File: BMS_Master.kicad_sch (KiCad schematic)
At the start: 24 parts, among them U1 STM32F103C8Tx, U2 AP2204K-ADJ, U3 AP2204K-ADJ, Y1 32.768k, Y2 8M

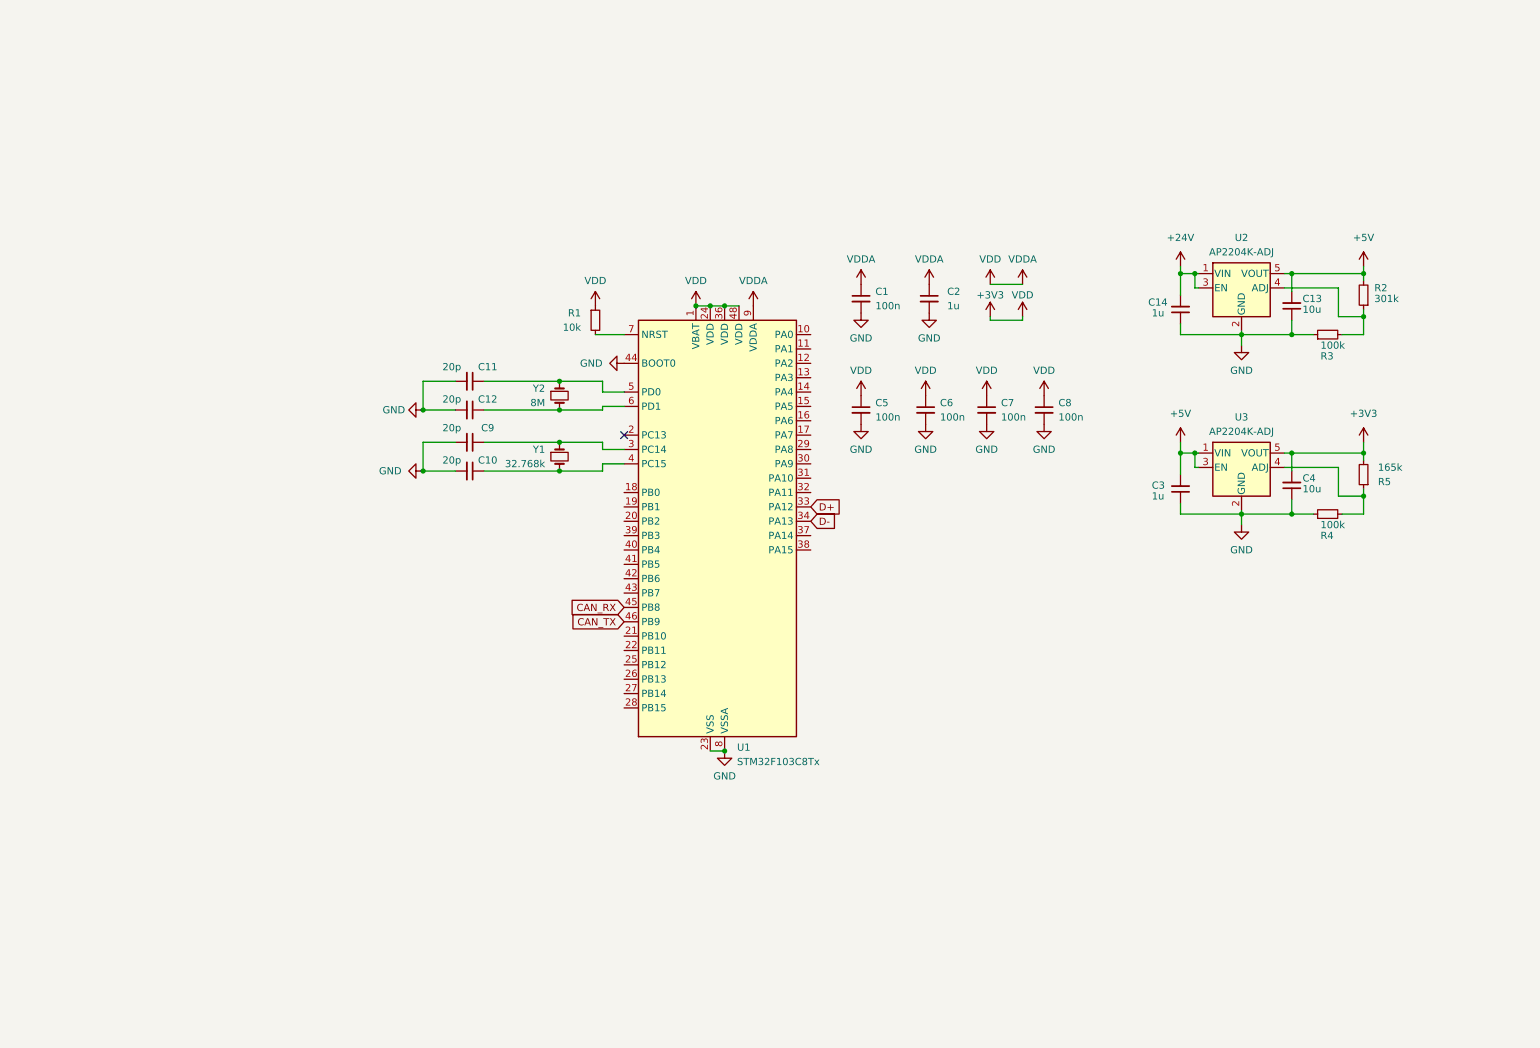
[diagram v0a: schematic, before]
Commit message: Add can bus transeiver and Readme.md
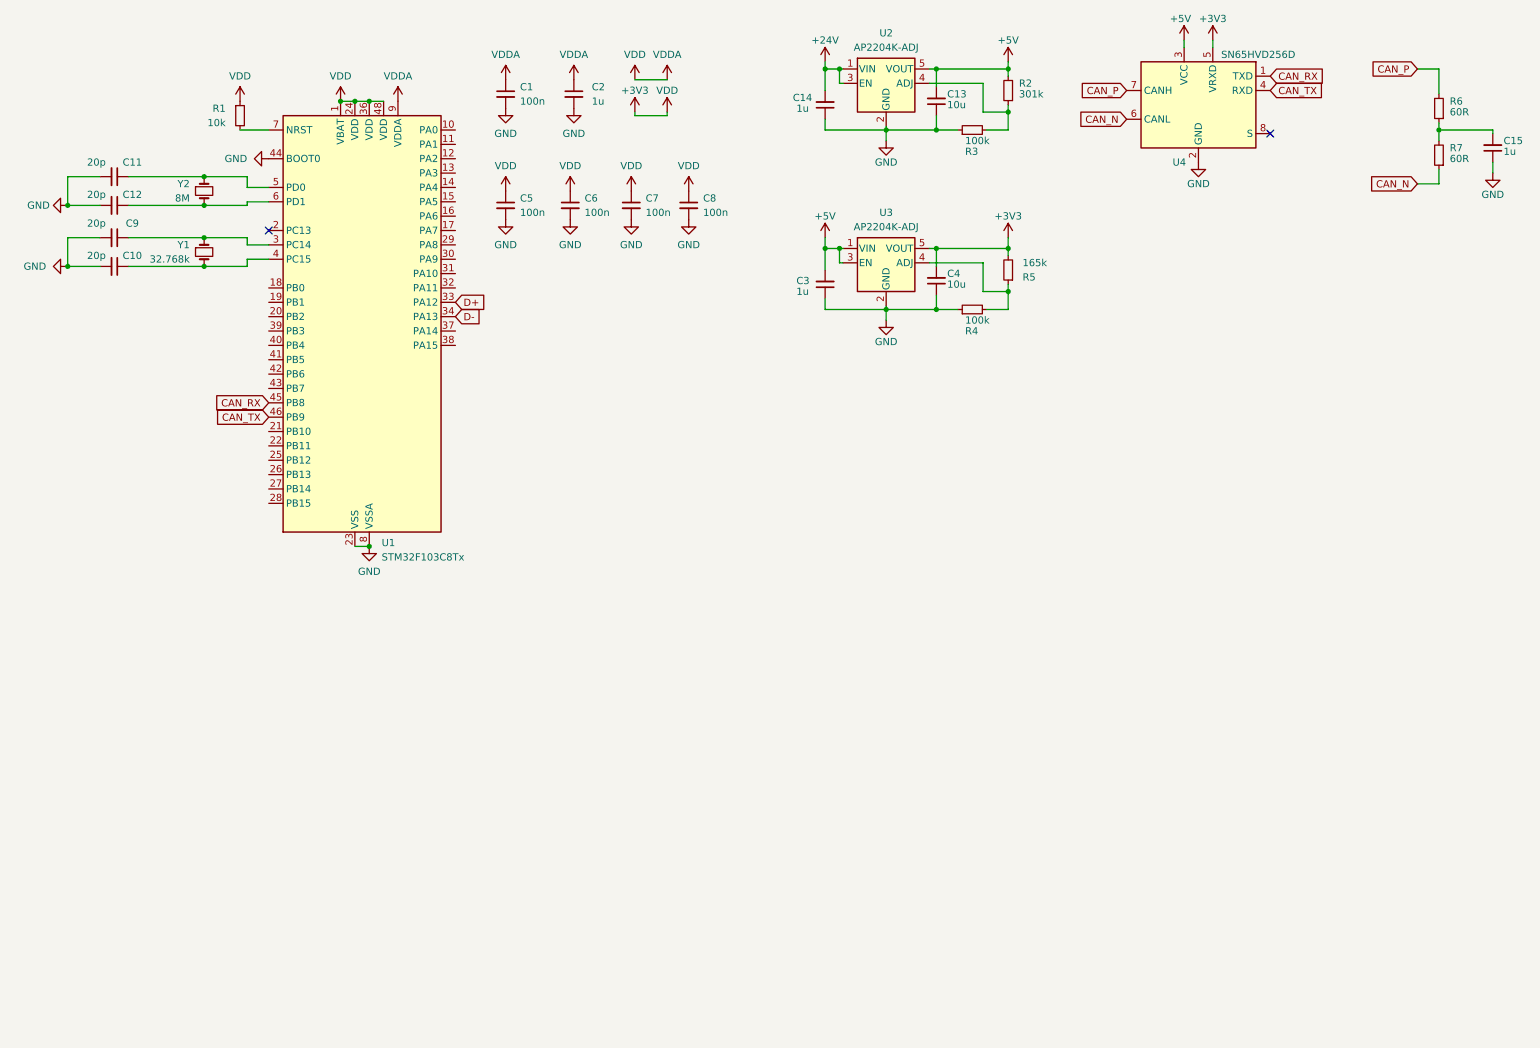
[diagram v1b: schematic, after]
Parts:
- added C15: 1u, Capacitor_SMD:C_0805_2012Metric, symbol Device:C_Small
- added R6, R7: 60R, Resistor_SMD:R_0603_1608Metric, symbol Device:R_Small
- added U4: SN65HVD256D, Package_SO:SOIC-8_3.9x4.9mm_P1.27mm, symbol Interface_CAN_LIN:SN65HVD256D
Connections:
- net +3V3: now also U4.5 (VRXD)
- net +5V: now also U4.3 (VCC)
- net CAN_RX: now also U4.1 (TXD)
- net CAN_TX: now also U4.4 (RXD)
- net GND: now also C15.1, U4.2 (GND)
- new net: C15.2, R6.1, R7.2
- new net CAN_N: R7.1, U4.6 (CANL)
- new net CAN_P: R6.2, U4.7 (CANH)
- no-connect marks 1 -> 2
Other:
- moved on the sheet: C1, C10, C11, C12, C13, C14, C2, C3, C4, C5, C6, C7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

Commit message: Finish schematic (probably)
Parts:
- added C16, C17: 220n, Capacitor_SMD:C_0805_2012Metric, symbol Device:C_Small
- added C18, C19, C22, C23: 220p, Capacitor_SMD:C_0603_1608Metric, symbol Device:C_Small
- added C20, C21: 100p, Capacitor_SMD:C_0603_1608Metric, symbol Device:C_Small
- added J1: BMS_M_OUT, Connector_Molex:Molex_Micro-Fit_3.0_43650-0200_1x02_P3.00mm_Horizontal, symbol Connector_Generic:Conn_01x02
- added J2: BMS_M_IN, Connector_Molex:Molex_Micro-Fit_3.0_43650-0200_1x02_P3.00mm_Horizontal, symbol Connector_Generic:Conn_01x02
- added J3: PWR, Connector_JST:JST_XH_S2B-XH-A_1x02_P2.50mm_Horizontal, symbol Connector_Generic:Conn_01x02
- added J4: CAN, Connector_JST:JST_XH_S3B-XH-A_1x03_P2.50mm_Horizontal, symbol Connector_Generic:Conn_01x03
- added J5: PROG, Connector_JST:JST_XH_S3B-XH-A_1x03_P2.50mm_Horizontal, symbol Connector_Generic:Conn_01x03
- added R10, R8, R9: 60R, Resistor_SMD:R_0603_1608Metric, symbol Device:R_Small
- added R11, R16: 1k, Resistor_SMD:R_0603_1608Metric, symbol Device:R_Small
- added R12, R13, R14, R15: 49R, Resistor_SMD:R_0603_1608Metric, symbol Device:R_Small
- added SW1: SW_SPST, symbol Switch:SW_SPST
- added TR1, TR2: Wuerth_750319696, Transformer_SMD:Transformer_Wuerth_750315371, symbol Transformer:Wuerth_750315371
- added U5: BQ79600-Q1, Package_SO:TSSOP-16_4.4x5mm_P0.65mm, symbol Local_Lib:BQ79600-Q1
- C1: footprint Capacitor_SMD:C_0805_2012Metric -> Package_SO:TSSOP-16-1EP_4.4x5mm_P0.65mm
- Y1, Y2: footprint (none) -> Crystal:Crystal_SMD_SeikoEpson_FA238-4Pin_3.2x2.5mm
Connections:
- net +24V: now also J3.1 (Pin_1), U5. (nUART/SPI(SPI_RDY))
- net CAN_N: now also J4.1 (Pin_1)
- net CAN_P: now also J4.3 (Pin_3)
- net D+: now also U1.32 (PA11); no longer U1.33 (PA12)
- net D-: now also U1.33 (PA12); no longer U1.34 (PA13)
- net GND: now also C16.2, C17.1, J3.2 (Pin_2), J5.3 (Pin_3), SW1.1 (A), U5. (nUART/SPI(SPI_RDY))
- net at R1.2, U1.7 (NRST): now also SW1.2 (B)
- net SWCLK: now reaches U1.37 (PA14)
- net SWCLK: now also J5.2 (Pin_2)
- new net: R13.2, TR2.3
- new net: R14.2, TR1.1
- new net: C20.1, TR1.2
- new net: R15.2, TR1.3
- new net: J1.2 (Pin_2), TR1.4
- new net: J1.1 (Pin_1), TR1.6
- new net: C16.1, U5. (nUART/SPI(SPI_RDY))
- new net: C17.2, U5. (nUART/SPI(SPI_RDY))
- new net: C21.1, TR2.2
- new net: J2.1 (Pin_1), TR2.6
- new net: J2.2 (Pin_2), TR2.4
- new net: R12.2, TR2.1
- new net COMHN: C23.1, R15.1, R16.2, U5. (nUART/SPI(SPI_RDY))
- new net COMHP: C22.1, R14.1, R16.1, U5. (nUART/SPI(SPI_RDY))
- new net COMLN: C19.1, R11.2, R13.1, U5. (nUART/SPI(SPI_RDY))
- new net COMLP: C18.1, R11.1, R12.1, U5. (nUART/SPI(SPI_RDY))
- new net GND1: C18.2, C19.2, C20.2, C21.2, C22.2, C23.2
- new net MISO: R9.2, U5. (nUART/SPI(SPI_RDY))
- new net MOSI: R8.2, U5. (nUART/SPI(SPI_RDY))
- new net NFAULT: R10.2, U5. (nUART/SPI(SPI_RDY))
- new net SWDIO: J5.1 (Pin_1), U1.34 (PA13)
- new net VIO: R10.1, R8.1, R9.1, U5. (nUART/SPI(SPI_RDY))
- no-connect marks 2 -> 5
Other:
- note added: "2mm Air Gap"
- moved on the sheet: C1, C10, C11, C12, C13, C14, C15, C2, C3, C4, C5, C6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

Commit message: Finish schematic (For real), for basic requirements
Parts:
- added C24: 220n, Capacitor_SMD:C_0603_1608Metric, symbol Device:C_Small
- added C25, C26: 100n, Capacitor_SMD:C_0603_1608Metric, symbol Device:C_Small
- added D1: RUN_GREEN, LED_SMD:LED_0805_2012Metric, symbol Device:LED
- added H1, H2, H3, H4: MountingHole_Pad, MountingHole:MountingHole_3.2mm_M3_ISO14580_Pad, symbol Mechanical:MountingHole_Pad
- added R17, R18: 10K, Resistor_SMD:R_0603_1608Metric, symbol Device:R_Small
- added R19: 100K, Resistor_SMD:R_0603_1608Metric, symbol Device:R_Small
- added R20: 1k, Resistor_SMD:R_0603_1608Metric, symbol Device:R_Small
- C1: footprint Package_SO:TSSOP-16-1EP_4.4x5mm_P0.65mm -> Capacitor_SMD:C_0603_1608Metric
- C10, C11, C12, C14, C15, C16, C17, C3, C5, C6, C7, C8, C9: footprint Capacitor_SMD:C_0805_2012Metric -> Capacitor_SMD:C_0603_1608Metric
- J3: footprint Connector_JST:JST_XH_S2B-XH-A_1x02_P2.50mm_Horizontal -> Connector_JST:JST_XH_B2B-XH-A_1x02_P2.50mm_Vertical
- J4, J5: footprint Connector_JST:JST_XH_S3B-XH-A_1x03_P2.50mm_Horizontal -> Connector_JST:JST_XH_B3B-XH-A_1x03_P2.50mm_Vertical
- R10: value 60R -> 100K
- R8, R9: value 60R -> 10K
- SW1: footprint (none) -> Button_Switch_SMD:SW_SPST_FSMSM
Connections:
- net GND1 is gone; now on net GND: C18.2, C19.2, C20.2, C21.2, C22.2, C23.2
- net +24V: no longer U5. (nUART/SPI(SPI_RDY))
- net +3V3: now also R10.1, R8.1, R9.1, U5.3 (VIO), C24.2, C26.2, R18.1, R19.1
- net +5V: now also C16.1, U5.14 (CVDD), U5.15 (BAT), U5.16 (INH), C25.2
- net COMHN: now also U5.12 (COMHN); no longer U5. (nUART/SPI(SPI_RDY))
- net COMHP: now also U5.13 (COMHP); no longer U5. (nUART/SPI(SPI_RDY))
- net COMLN: now also U5.11 (COMLN); no longer U5. (nUART/SPI(SPI_RDY))
- net COMLP: now also U5.10 (COMLP); no longer U5. (nUART/SPI(SPI_RDY))
- net GND: now also U1.15 (PA5), U5.9 (GND), C24.1, C25.1, C26.1, D1.1 (K), H1.1, H2.1, H3.1, H4.1, R17.2; no longer U5. (nUART/SPI(SPI_RDY))
- net MISO: now also U1.16 (PA6), U5.5 (MISO/TX); no longer U5. (nUART/SPI(SPI_RDY))
- net MOSI: now also U1.17 (PA7), U5.4 (MOSI/RX); no longer U5. (nUART/SPI(SPI_RDY))
- net NFAULT: now also U1.27 (PB14), U5.2 (NFAULT); no longer U5. (nUART/SPI(SPI_RDY))
- net at C17.2: now also U5.1 (DVDD); no longer U5. (nUART/SPI(SPI_RDY))
- net nCS: now reaches U1.14 (PA4)
- net nCS: now also U5.7 (nCS), R18.2
- net RUN_LED: now reaches U1.2 (PC13)
- net RUN_LED: now also R20.2
- net SPI_RDY: now reaches U1.28 (PB15)
- net SPI_RDY: now also U5.8 (nUART/SPI(SPI_RDY)), R19.2
- removed net VIO: R10.1, R8.1, R9.1, U5. (nUART/SPI(SPI_RDY))
- new net: R17.1, U5.6 (SCLK)
- new net: D1.2 (A), R20.1
- no-connect marks 5 -> 24
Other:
- note added: "BMS_Transceiver"
- note added: "CAN_Transceiver"
- note added: "MCU"
- note added: "Mount"
- note added: "Power"
- company: (none) -> NCKU Formula SAE
- title: (none) -> BMS Master
- moved on the sheet: C1, C10, C11, C12, C13, C14, C15, C16, C17, C18, C19, C2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

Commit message: Initiate PCB layout and make some arrangement in Schematic
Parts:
- removed R17: 10K, Resistor_SMD:R_0603_1608Metric, symbol Device:R_Small
- removed Y1: 32.768k, Crystal:Crystal_SMD_SeikoEpson_FA238-4Pin_3.2x2.5mm, symbol Device:Crystal_Small
- removed Y2: 8M, Crystal:Crystal_SMD_SeikoEpson_FA238-4Pin_3.2x2.5mm, symbol Device:Crystal_Small
- added D1: PWR_Yellow, LED_SMD:LED_0805_2012Metric, symbol Device:LED
- added D3: FAULT_RED, LED_SMD:LED_0805_2012Metric, symbol Device:LED
- added Q1: BC807, Package_TO_SOT_SMD:SOT-23, symbol Transistor_BJT:BC807
- added R1: 1k, Resistor_SMD:R_0603_1608Metric, symbol Device:R_Small
- added R20, R8: 10K, Resistor_SMD:R_0603_1608Metric, symbol Device:R_Small
- added Y1: 8M, Crystal:Crystal_SMD_SeikoEpson_FA238-4Pin_3.2x2.5mm, symbol Device:Crystal_GND24_Small
- added Y2: 32.768k, Crystal:Crystal_SMD_SeikoEpson_FA238-4Pin_3.2x2.5mm, symbol Device:Crystal_GND24_Small
- renumbered C14 to C1, C1 to C10, C6 to C11, C2 to C12, C7 to C13, C8 to C14, C24 to C15, C17 to C16, C22 to C17, C23 to C18, C18 to C19, C3 to C2, C19 to C20, C20 to C21, C21 to C22, C16 to C23, C25 to C24, C26 to C25, C15 to C26, C13 to C3, C11 to C5, C12 to C6, C9 to C7, C10 to C8, C5 to C9, D1 to D2, J3 to J1, J5 to J2, J1 to J3, J2 to J4, J4 to J5, R11 to R10, R8 to R11, R9 to R12, R18 to R13, R19 to R14, R10 to R15, R14 to R16, R15 to R17, R12 to R18, R13 to R19, R3 to R2, R6 to R21, R7 to R22, R4 to R3, R2 to R4, R1 to R6, R20 to R7, R16 to R9, U2 to U1, U3 to U2, U1 to U3, U5 to U4, U4 to U5
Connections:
- net +3V3: now also Q1.2 (E), R1.2
- net GND: now also D1.1 (K), D3.1 (K), R8.2, Y1.2, Y1.4, Y2.2, Y2.4; no longer U3.15 (PA5)
- net SCLK: now reaches U4.6 (SCLK)
- net SCLK: now also U3.15 (PA5), R8.1
- net at C5.1, U3.5 (PD0): now also Y1.3
- net at C6.1, U3.6 (PD1): now also Y1.1
- net at C7.1, U3.3 (PC14): now also Y2.3
- net at C8.1, U3.4 (PC15): now also Y2.1
- net BMS_FAULT: now reaches U3.12 (PA2)
- net BMS_FAULT: now also R20.2
- net D+: no longer names the net of U3.32 (PA11)
- net D-: no longer names the net of U3.33 (PA12)
- new net: D1.2 (A), R1.1
- new net: Q1.1 (B), R20.1
- new net: D3.2 (A), Q1.3 (C)
- no-connect marks 24 -> 25
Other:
- moved on the sheet: C1, C10, C11, C12, C13, C14, C15, C2, C24, C25, C26, C3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

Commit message: Finish PCB layout Ver 1.0
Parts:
- removed C12: 1u, Capacitor_SMD:C_0603_1608Metric, symbol Device:C_Small
- J2: footprint Connector_JST:JST_XH_B3B-XH-A_1x03_P2.50mm_Vertical -> Connector_PinHeader_2.54mm:PinHeader_1x03_P2.54mm_Vertical
- renumbered C11 to C10, C10 to C11, C13 to C12, C14 to C13, C15 to C14, C16 to C15, C17 to C16, C18 to C17, C19 to C18, C20 to C19, C21 to C20, C22 to C21, C23 to C22, C24 to C23, C25 to C24, C26 to C25
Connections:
- net CAN_N: now also J5.3 (Pin_3); no longer J5.1 (Pin_1)
- net CAN_P: now also J5.1 (Pin_1); no longer J5.3 (Pin_3)
- net at R19.2: now also TR2.1; no longer TR2.3
- net at J4.1 (Pin_1): now also TR2.4; no longer TR2.6
- net at J4.2 (Pin_2): now also TR2.6; no longer TR2.4
- net at R18.2: now also TR2.3; no longer TR2.1
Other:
- moved on the sheet: C11, C23, C24, C25, J5, R21, R22, U5

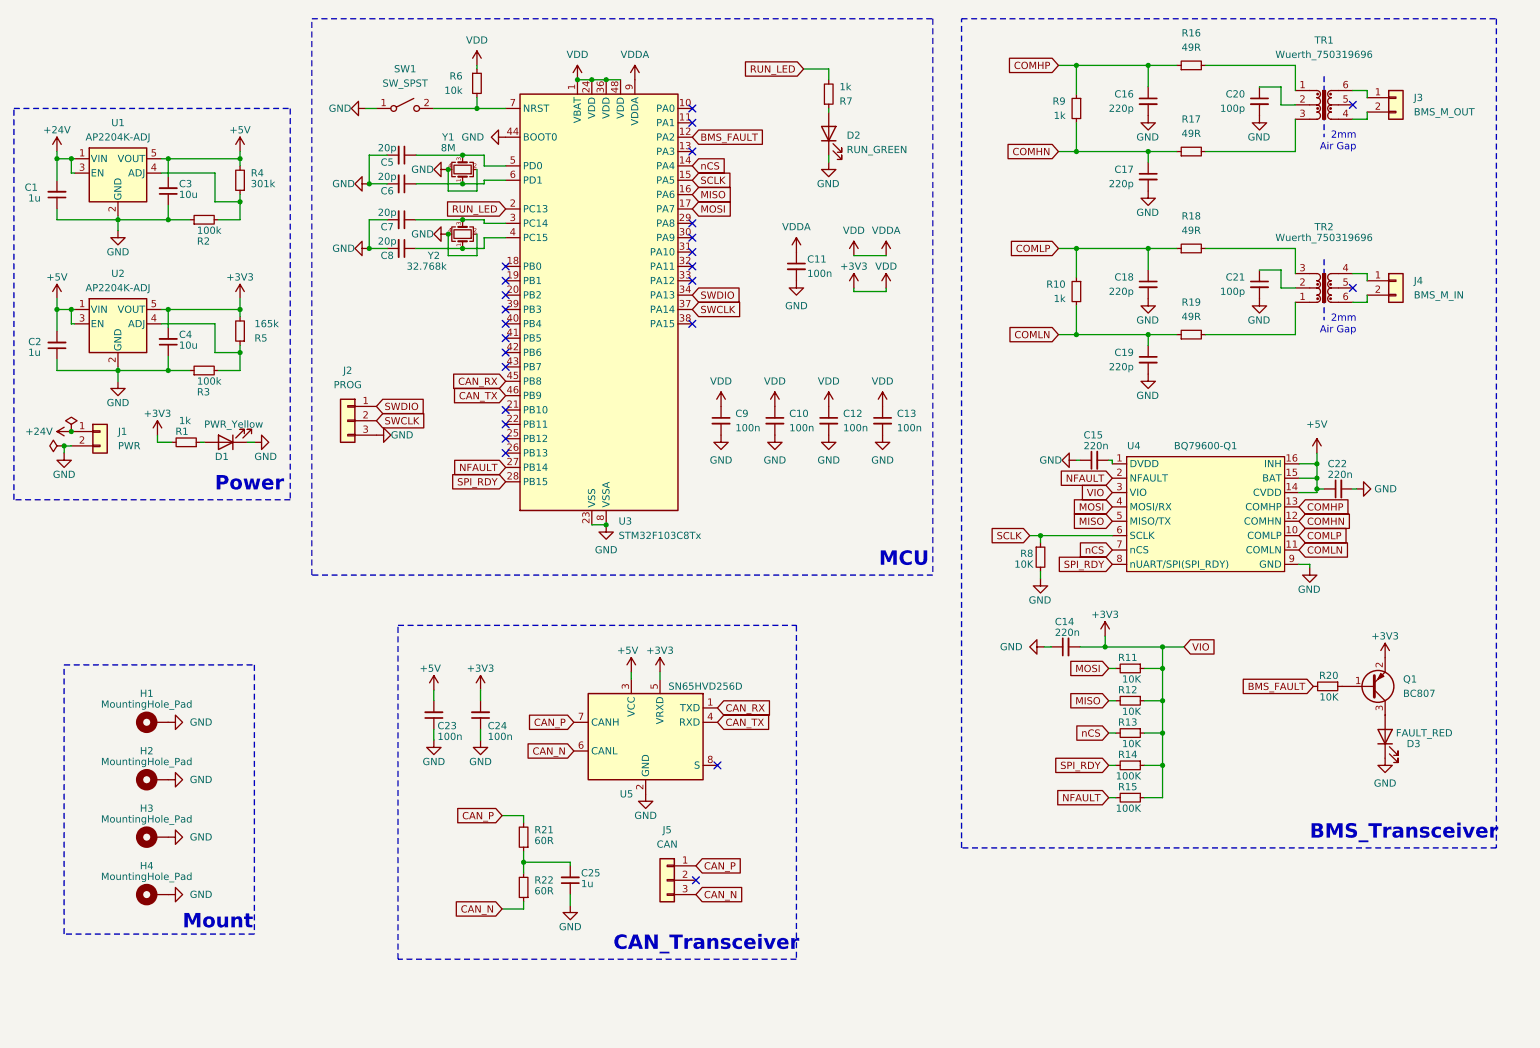
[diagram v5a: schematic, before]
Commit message: Fix layout problems
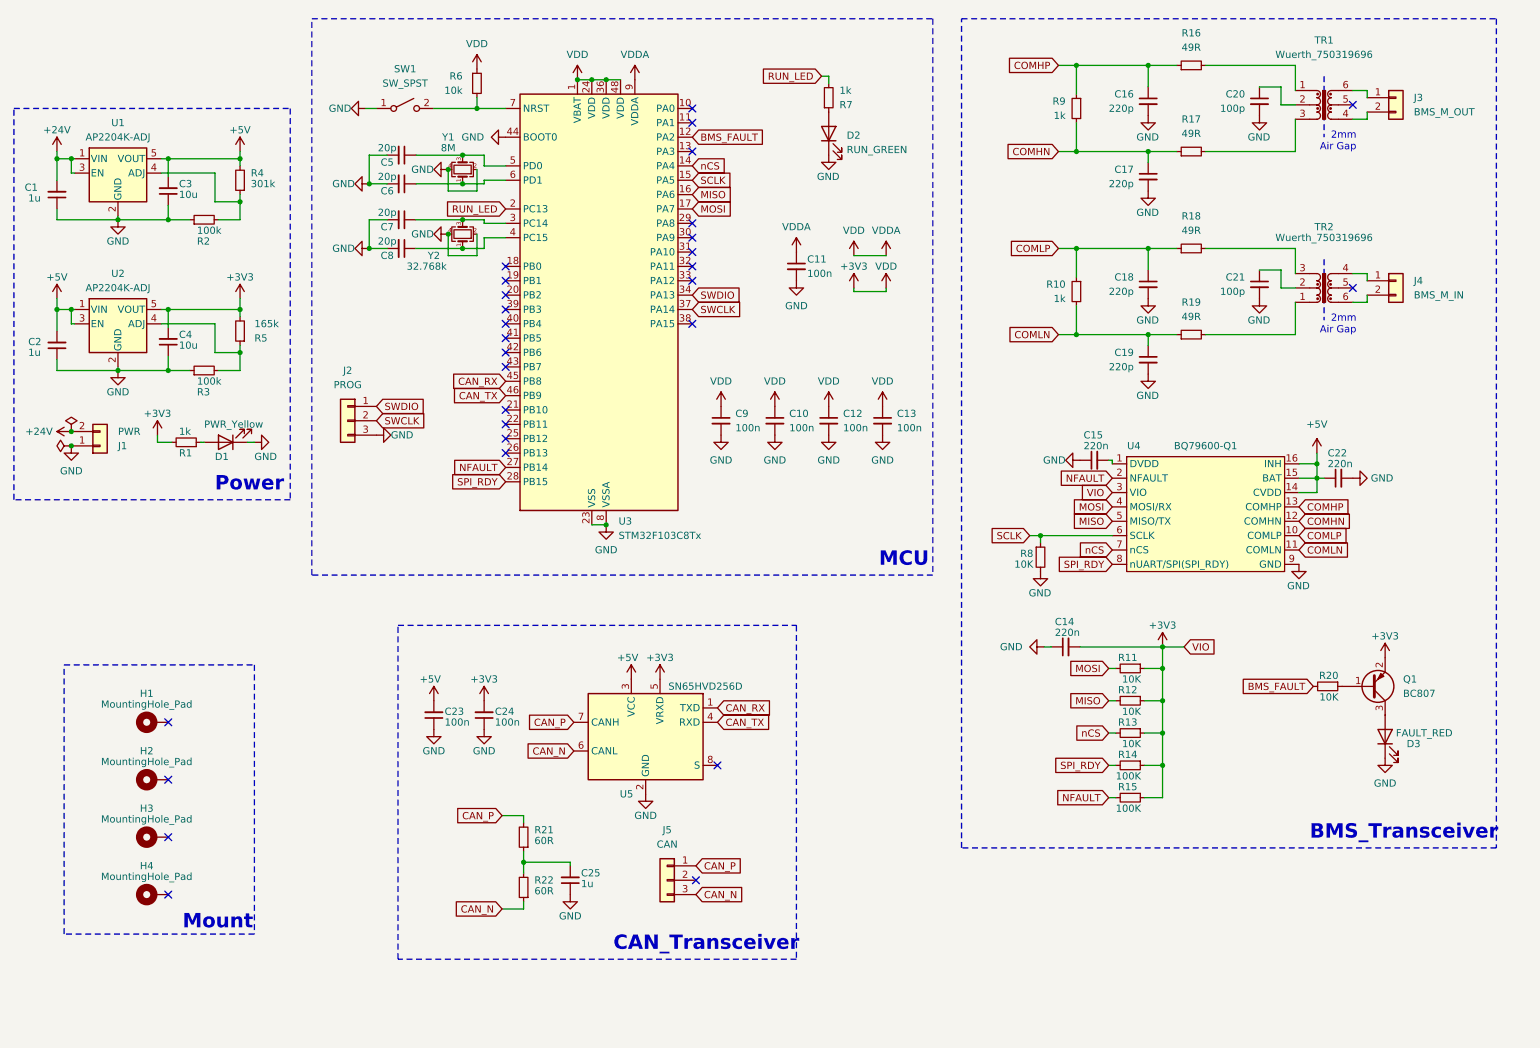
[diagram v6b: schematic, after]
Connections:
- net +24V: now also J1.2 (Pin_2); no longer J1.1 (Pin_1)
- net GND: now also J1.1 (Pin_1); no longer H1.1, H2.1, H3.1, H4.1, J1.2 (Pin_2)
- no-connect marks 25 -> 29
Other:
- moved on the sheet: C22, C24, R7
